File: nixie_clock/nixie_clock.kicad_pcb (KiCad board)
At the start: 2 copper layers, 147.3 x 90.2 mm, 52 parts, among them P1 CONN_01X04, P10 CONN_01X03, P11 CONN_01X02, P12 CONN_01X03, P13 CONN_01X02, P2 CONN_01X03, P3 CONN_01X02, P4 CONN_01X03, P5 CONN_01X02, P6 CONN_01X03, P7 CONN_01X02, P8 CONN_01X03, P9 CONN_01X02, U1 4518, U10 K155ID1, U11 IN-12, U12 4518, U13 4011, U14 K155ID1, U15 IN-12, U16 K155ID1, U17 IN-12, U2 4011, U3 K155ID1, U4 IN-12, U5 K155ID1, U6 IN-12, U7 4518, U8 K155ID1, U9 IN-12

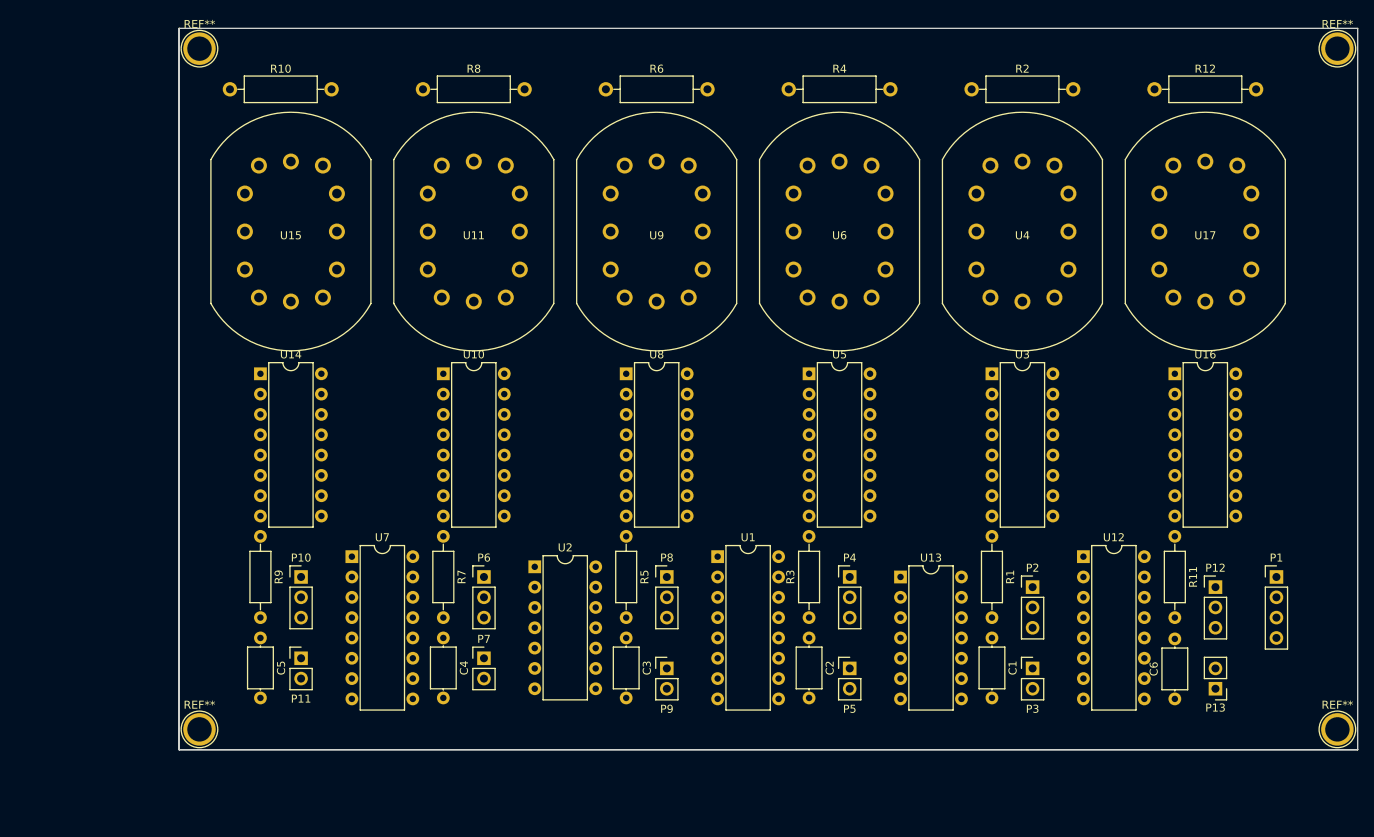
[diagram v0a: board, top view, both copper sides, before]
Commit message: Started routing for the clock
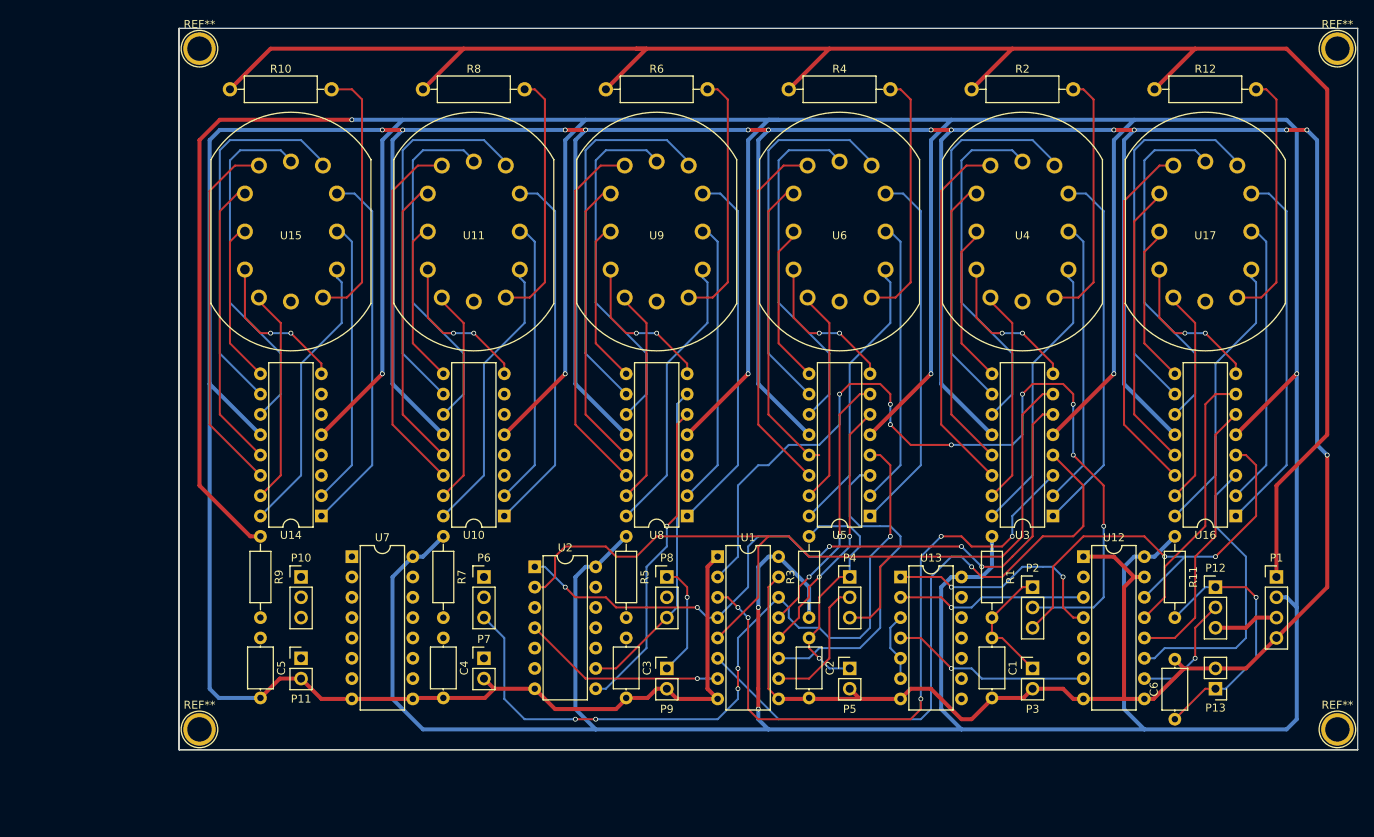
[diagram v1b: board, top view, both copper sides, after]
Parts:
- moved U10 19.3 mm to (116.8, 82.5), turned to 180 degrees
- moved U14 19.3 mm to (94.0, 82.5), turned to 180 degrees
- moved U16 19.3 mm to (208.3, 82.5), turned to 180 degrees
- moved U5 19.3 mm to (162.6, 82.5), turned to 180 degrees
- moved U3 19.3 mm to (185.4, 82.5), turned to 180 degrees
- moved U8 19.3 mm to (139.7, 82.5), turned to 180 degrees
- moved C6 2.54 mm to (200.7, 108.0)
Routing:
- net +5V: track 0.00 -> 758.7 mm, vias 0 -> 9
- net GND: track 0.00 -> 692.6 mm, vias 0 -> 13
- net +220V: track 0.00 -> 242.1 mm
- net /1minute/CLK_IN: track 0.00 -> 114.9 mm
- net Net-(P2-Pad2): track 0.00 -> 110.3 mm, vias 0 -> 8
- net /10minute/CLK_IN: track 0.00 -> 96.6 mm, vias 0 -> 5
- net Net-(U1-Pad4): track 0.00 -> 93.3 mm, vias 0 -> 5
- net Net-(U1-Pad3): track 0.00 -> 83.8 mm, vias 0 -> 5
- net Net-(U1-Pad6): track 0.00 -> 81.1 mm, vias 0 -> 1
- net /10second/CLK_IN: track 0.00 -> 55.4 mm, vias 0 -> 2
- net Net-(U3-Pad10): track 0.00 -> 47.6 mm
- net Net-(U14-Pad10): track 0.00 -> 47.6 mm
- net Net-(U10-Pad10): track 0.00 -> 47.6 mm
- net Net-(U8-Pad10): track 0.00 -> 47.6 mm
- net Net-(U5-Pad10): track 0.00 -> 47.6 mm
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
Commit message: Finished routing
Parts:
- moved REF** 2.54 mm to (221.0, 111.8)
- moved REF** 2.54 mm to (78.7, 111.8)
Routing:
- net Net-(U12-Pad5): track 0.00 -> 180.0 mm, vias 0 -> 3
- net Net-(U12-Pad4): track 29.3 -> 202.9 mm, vias 2 -> 6
- net Net-(U12-Pad6): track 0.00 -> 166.2 mm, vias 0 -> 6
- net Net-(P10-Pad2): track 0.00 -> 136.2 mm, vias 0 -> 3
- net Net-(U12-Pad3): track 23.9 -> 142.5 mm, vias 1 -> 3
- net Net-(U7-Pad6): track 0.00 -> 60.8 mm, vias 0 -> 2
- net /1hour/CLK_IN: track 40.5 -> 99.9 mm, vias 0 -> 9
- net Net-(U7-Pad3): track 0.00 -> 57.6 mm, vias 0 -> 3
- net Net-(U2-Pad11): track 0.00 -> 44.3 mm, vias 0 -> 2
- net Net-(U2-Pad8): track 39.8 -> 83.8 mm, vias 1 -> 5
- net Net-(C4-Pad1): track 14.3 -> 57.1 mm, vias 1 -> 3
- net /10hour/CLK_IN: track 0.00 -> 39.0 mm
- net Net-(C3-Pad1): track 0.00 -> 36.2 mm, vias 0 -> 2
- net Net-(P8-Pad2): track 0.00 -> 36.0 mm, vias 0 -> 2
- net Net-(U10-Pad7): track 0.00 -> 34.2 mm, vias 0 -> 1
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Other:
- board size 147.3 x 90.2 mm -> 147.3 x 92.7 mm

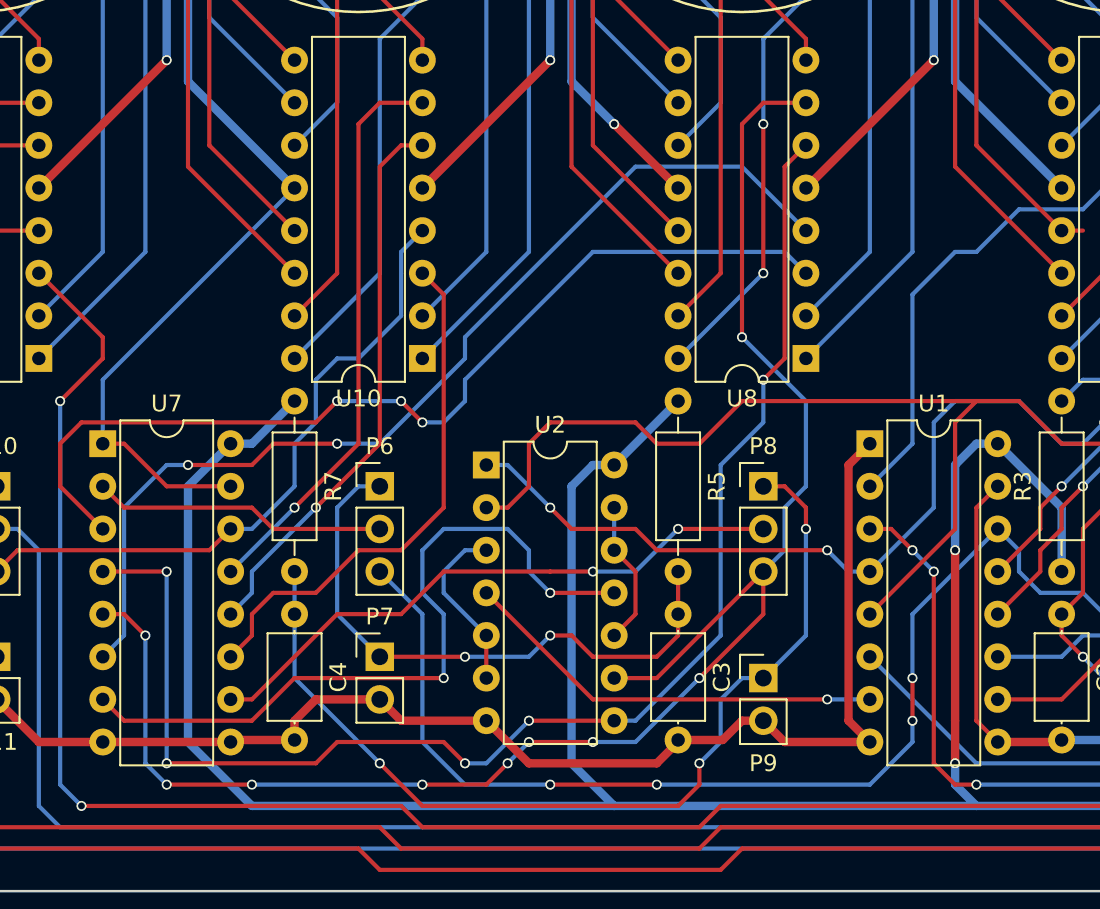
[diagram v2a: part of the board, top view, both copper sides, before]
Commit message: I had the 10 minute and 1 hour setting connectors mixed up
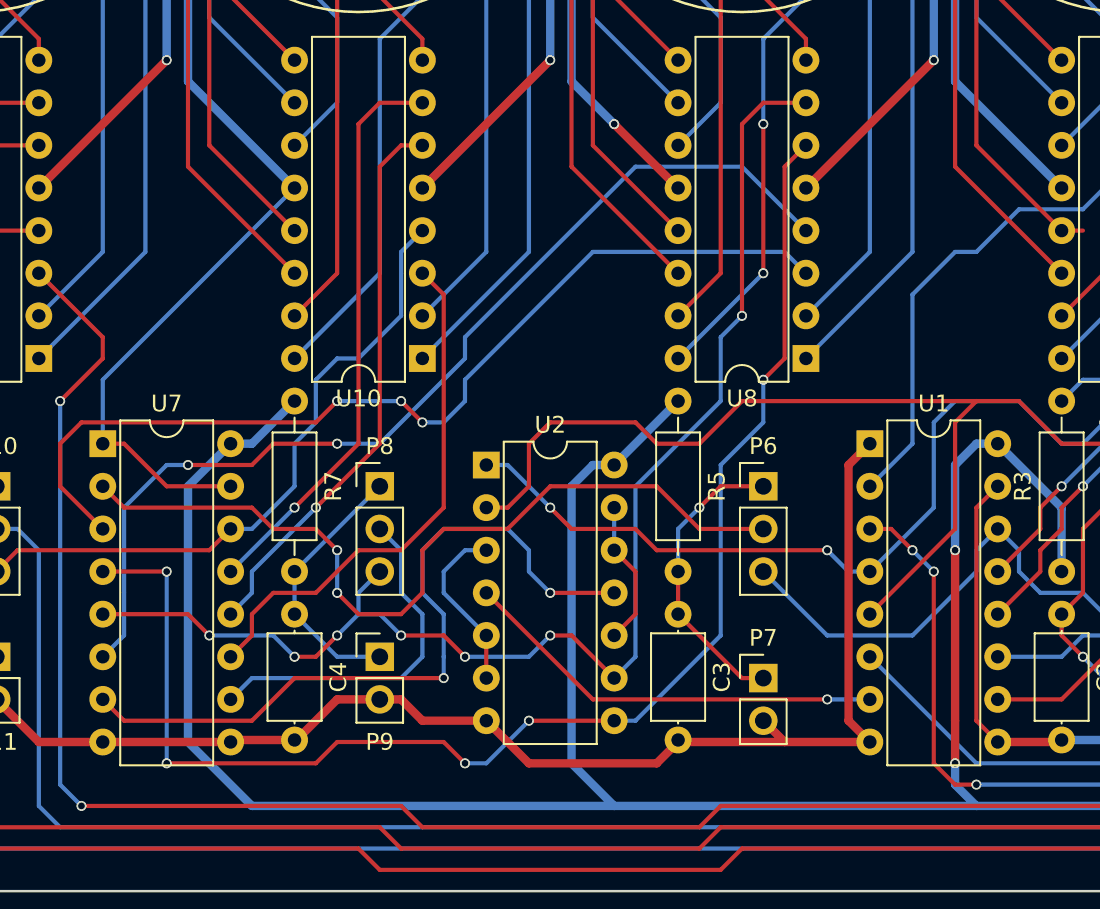
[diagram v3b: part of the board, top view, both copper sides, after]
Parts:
- moved P7 22.9 mm to (137.2, 101.6)
- moved P9 22.9 mm to (114.3, 100.3)
- moved P6 22.9 mm to (137.2, 90.2)
- moved P8 22.9 mm to (114.3, 90.2)
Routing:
- net Net-(C4-Pad1): track 57.1 -> 15.9 mm, vias 3 -> 0
- net /10minute/CLK_IN: track 96.6 -> 58.2 mm, vias 5 -> 1
- net Net-(P6-Pad2): track 17.6 -> 49.7 mm, vias 0 -> 2
- net /1hour/CLK_IN: track 99.9 -> 78.8 mm, vias 9 -> 7
- net Net-(C3-Pad1): track 36.2 -> 17.9 mm, vias 2 -> 1
- net Net-(P8-Pad2): track 36.0 -> 21.2 mm, vias 2 -> 0

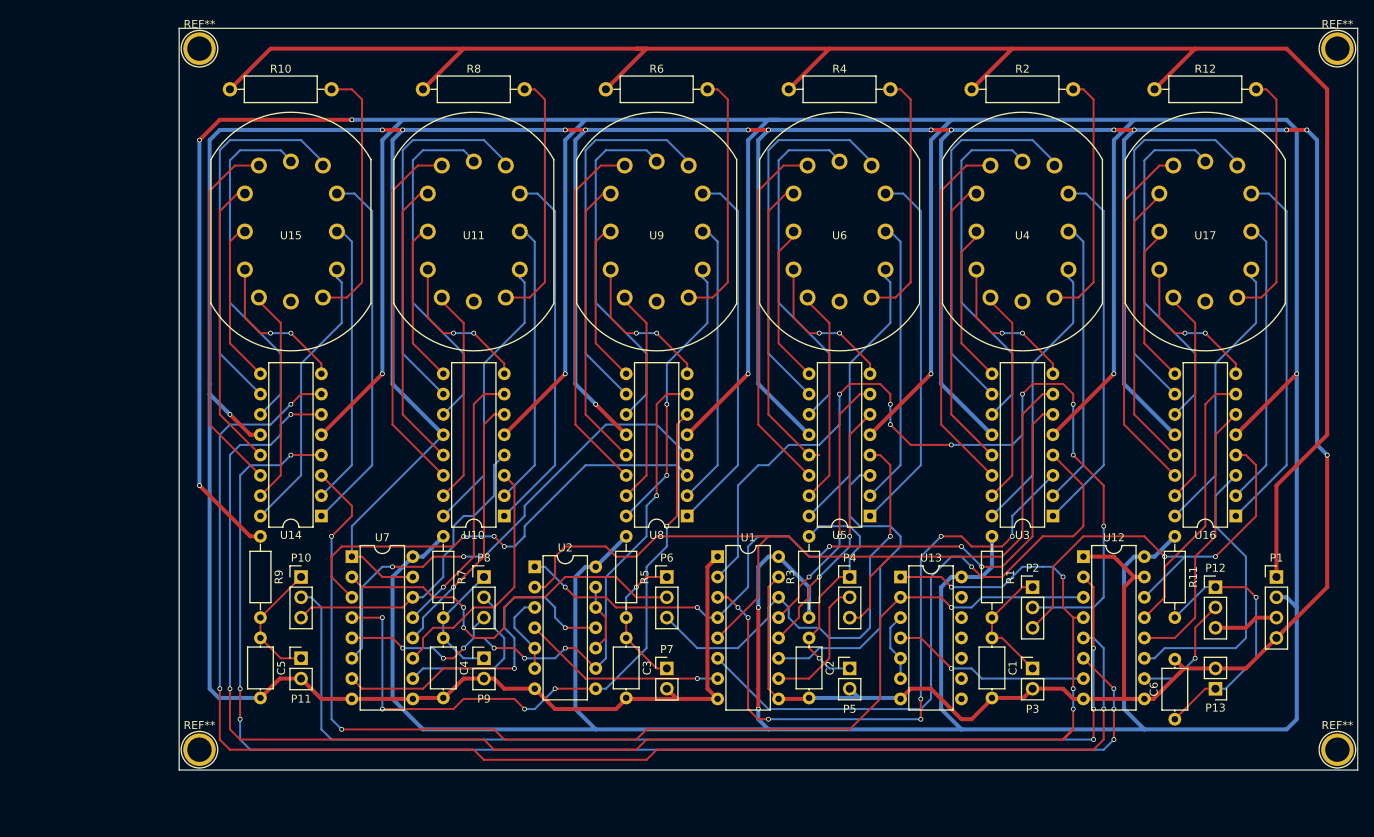
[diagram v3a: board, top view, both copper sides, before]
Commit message: Supply board mk2: reduced time base noise, upped some clearances, added ground plane
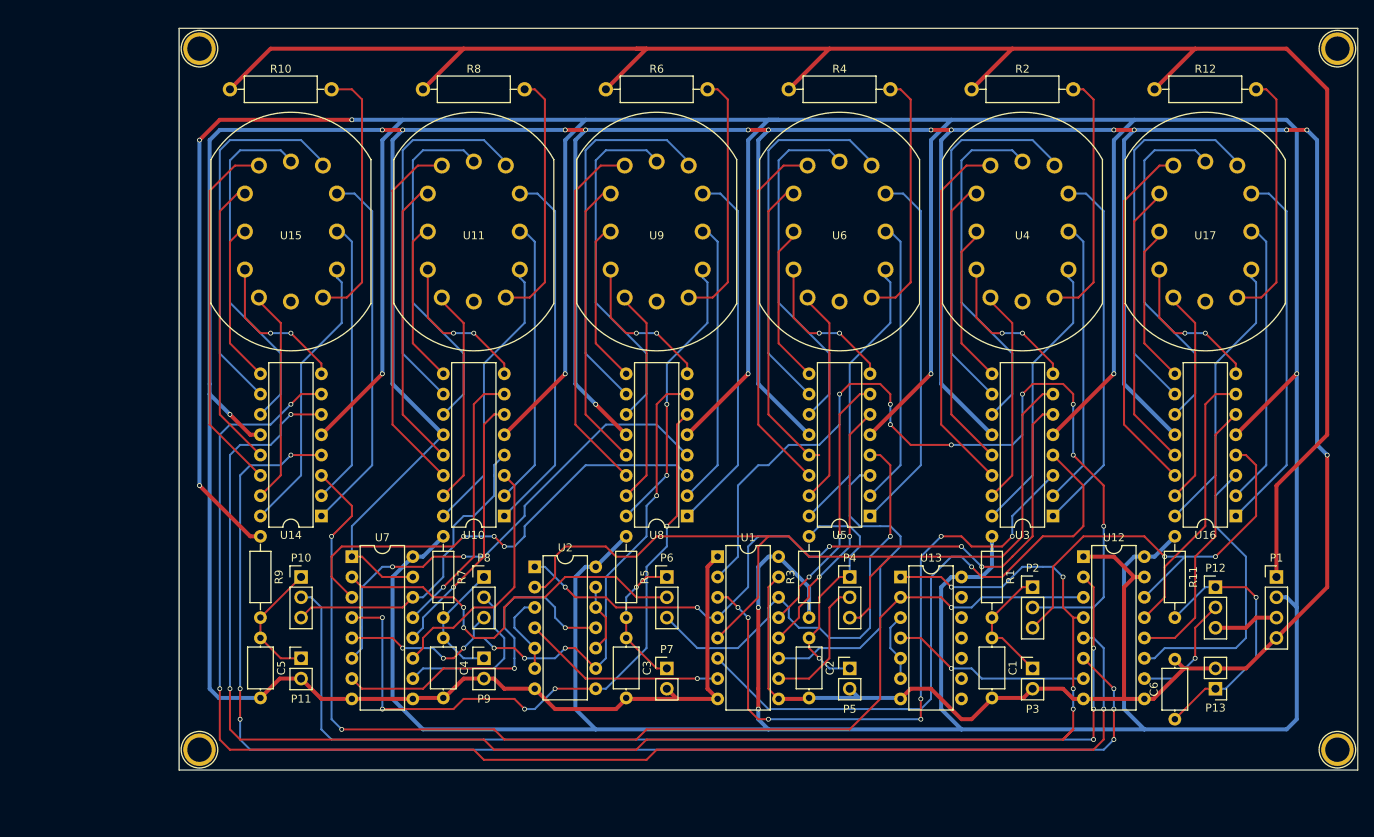
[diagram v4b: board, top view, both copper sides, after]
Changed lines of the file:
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@@
     (links 190)
     (no_connects 0)
-    (area 72.104999 20.107 223.805001 115.835)
+    (area 75.914999 20.107 223.805001 115.835)
     (thickness 1.6)
     (drawings 4)
@@
     (mod_text_size 1 1)
     (mod_text_width 0.15)
-    (pad_size 1.524 1.524)
-    (pad_drill 0.762)
+    (pad_size 2 2)
+    (pad_drill 1.2)
     (pad_to_mask_clearance 0.2)
     (aux_axis_origin 0 0)
     (visible_elements FFFFFF7F)
     (pcbplotparams
-      (layerselection 0x00030_80000001)
+      (layerselection 0x010e0_80000001)
       (usegerberextensions false)
       (excludeedgelayer true)
@@
       (outputformat 1)
       (mirror false)
-      (drillshape 1)
+      (drillshape 0)
       (scaleselection 1)
-      (outputdirectory ""))
+      (outputdirectory gerber/))
   )
   (net 0 "")
@@
     (descr "module 1 pin (ou trou mecanique de percage)")
     (tags DEV)
-    (fp_text reference REF** (at 0 -3.048) (layer F.SilkS)
+    (fp_text reference REF** (at 0 -3.048) (layer F.SilkS) hide
       (effects (font (size 1 1) (thickness 0.15)))
     )
@@
     (descr "module 1 pin (ou trou mecanique de percage)")
     (tags DEV)
-    (fp_text reference REF** (at 0 -3.048) (layer F.SilkS)
+    (fp_text reference REF** (at 0 -3.048) (layer F.SilkS) hide
       (effects (font (size 1 1) (thickness 0.15)))
     )
@@
     (descr "module 1 pin (ou trou mecanique de percage)")
     (tags DEV)
-    (fp_text reference REF** (at 0 -3.048) (layer F.SilkS)
+    (fp_text reference REF** (at 0 -3.048) (layer F.SilkS) hide
       (effects (font (size 1 1) (thickness 0.15)))
     )
@@
     (descr "module 1 pin (ou trou mecanique de percage)")
     (tags DEV)
-    (fp_text reference REF** (at 0 -3.048) (layer F.SilkS)
-      (effects (font (size 1 1) (thickness 0.15)))
-    )
+    (fp_text reference REF** (at 0 -3.048) (layer F.SilkS) hide
+      (effects (font (size 1 1) (thickness 0.15)))
+    )
